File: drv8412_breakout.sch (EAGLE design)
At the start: 1 part

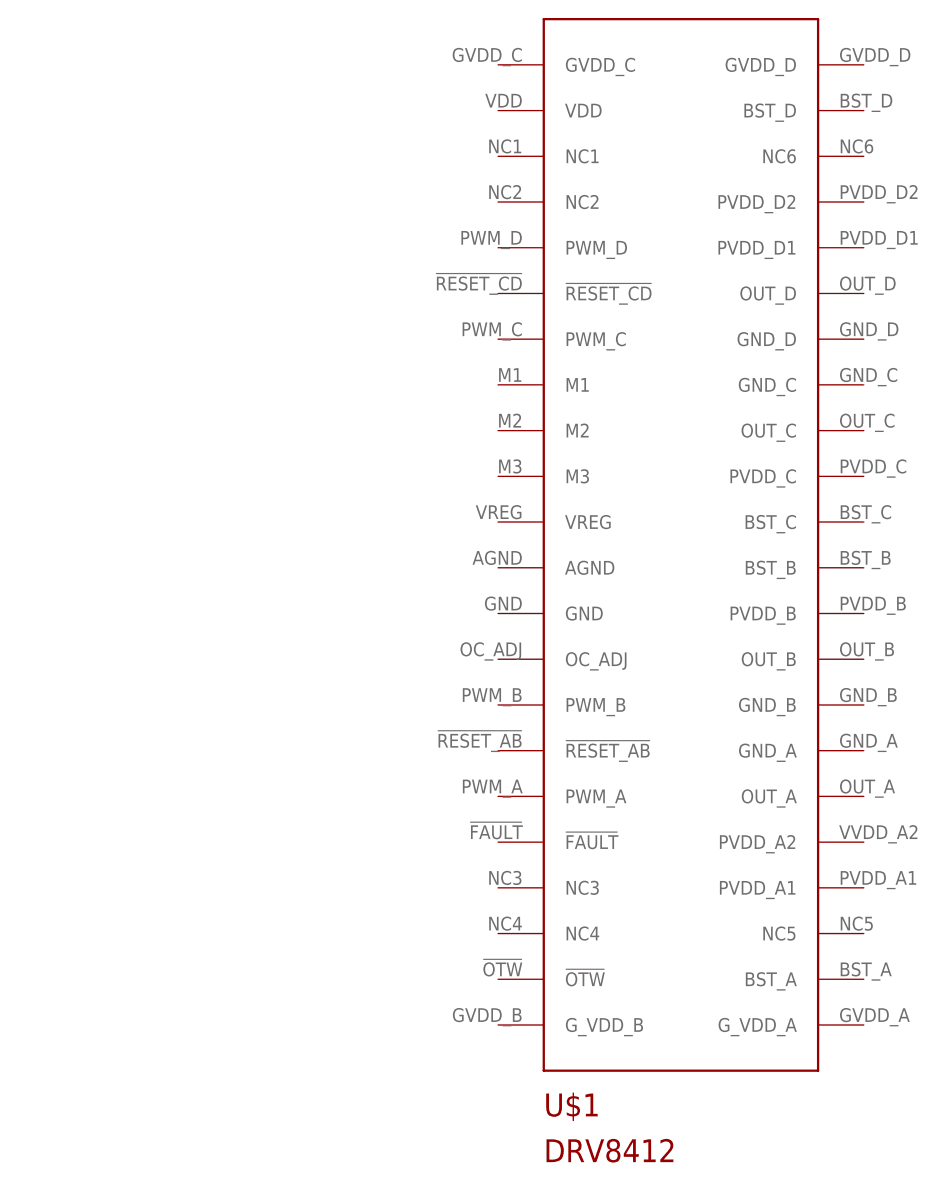
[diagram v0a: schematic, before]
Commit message: Added schematic and board layout
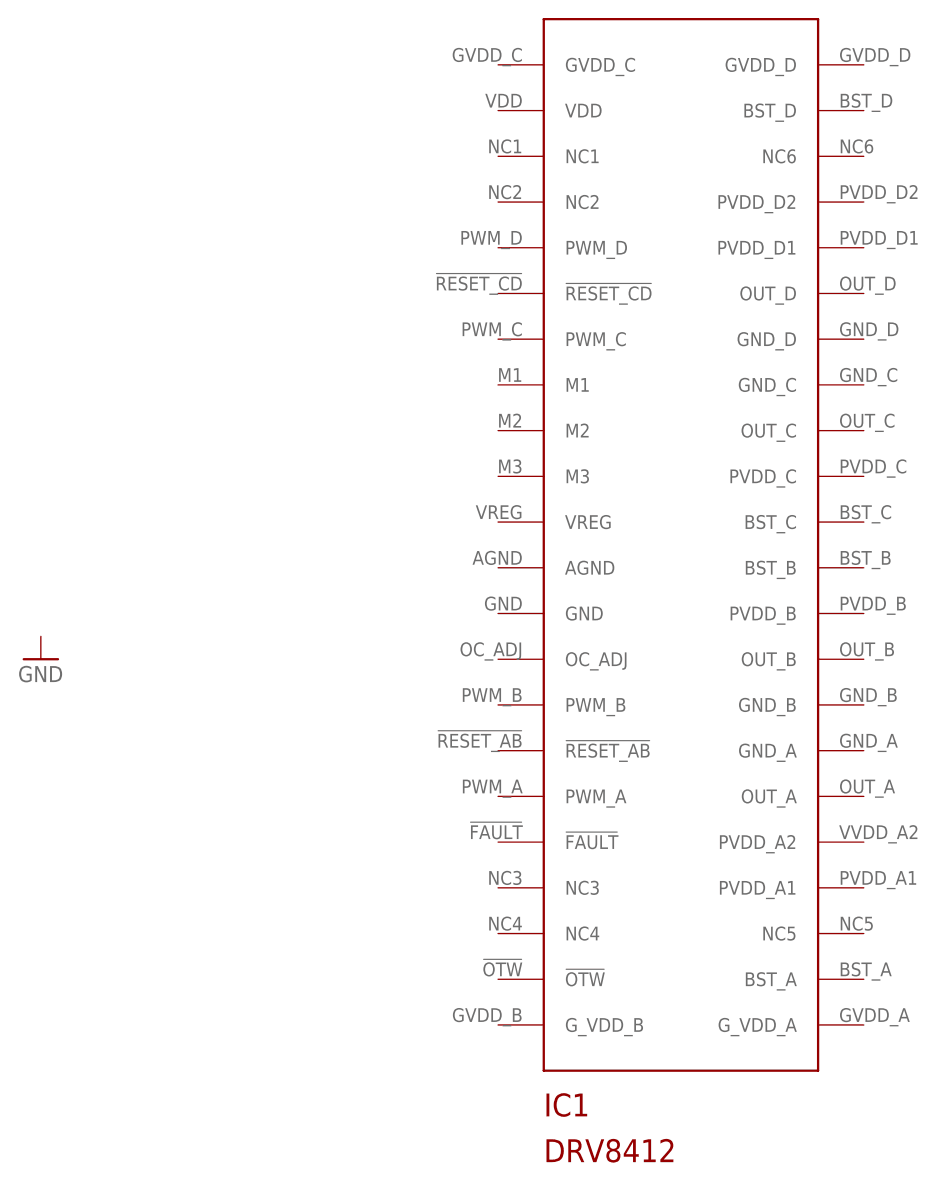
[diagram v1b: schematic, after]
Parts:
- renumbered U$1 to IC1
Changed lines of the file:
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@@
 <layer number="48" name="Document" color="7" fill="1" visible="no" active="no"/>
 <layer number="49" name="Reference" color="7" fill="1" visible="no" active="no"/>
+<layer number="50" name="dxf" color="7" fill="1" visible="no" active="no"/>
 <layer number="51" name="tDocu" color="7" fill="1" visible="no" active="no"/>
 <layer number="52" name="bDocu" color="7" fill="1" visible="no" active="no"/>
+<layer number="53" name="tGND_GNDA" color="7" fill="9" visible="no" active="no"/>
+<layer number="54" name="bGND_GNDA" color="1" fill="9" visible="no" active="no"/>
+<layer number="56" name="wert" color="7" fill="1" visible="no" active="no"/>
 <layer number="90" name="Modules" color="5" fill="1" visible="yes" active="yes"/>
 <layer number="91" name="Nets" color="2" fill="1" visible="yes" active="yes"/>
@@
 <layer number="97" name="Info" color="7" fill="1" visible="yes" active="yes"/>
 <layer number="98" name="Guide" color="6" fill="1" visible="yes" active="yes"/>
+<layer number="100" name="Muster" color="7" fill="1" visible="no" active="no"/>
+<layer number="101" name="Patch_Top" color="12" fill="4" visible="yes" active="yes"/>
+<layer number="102" name="Vscore" color="7" fill="1" visible="yes" active="yes"/>
+<layer number="103" name="tMap" color="7" fill="1" visible="yes" active="yes"/>
+<layer number="104" name="Name" color="16" fill="1" visible="yes" active="yes"/>
+<layer number="105" name="tPlate" color="7" fill="1" visible="yes" active="yes"/>
+<layer number="106" name="bPlate" color="7" fill="1" visible="yes" active="yes"/>
+<layer number="107" name="Crop" color="7" fill="1" visible="yes" active="yes"/>
+<layer number="108" name="tplace-old" color="10" fill="1" visible="no" active="yes"/>
+<layer number="109" name="ref-old" color="11" fill="1" visible="no" active="yes"/>
+<layer number="116" name="Patch_BOT" color="9" fill="4" visible="yes" active="yes"/>
+<layer number="121" name="_tsilk" color="7" fill="1" visible="yes" active="yes"/>
+<layer number="122" name="_bsilk" color="7" fill="1" visible="yes" active="yes"/>
+<layer number="125" name="_tNames" color="7" fill="1" visible="yes" active="yes"/>
+<layer number="144" name="Drill_legend" color="7" fill="1" visible="yes" active="yes"/>
+<layer number="151" name="HeatSink" color="7" fill="1" visible="yes" active="yes"/>
+<layer number="199" name="Contour" color="7" fill="1" visible="yes" active="yes"/>
+<layer number="200" name="200bmp" color="1" fill="10" visible="yes" active="yes"/>
+<layer number="201" name="201bmp" color="2" fill="10" visible="yes" active="yes"/>
+<layer number="202" name="202bmp" color="3" fill="10" visible="yes" active="yes"/>
+<layer number="203" name="203bmp" color="4" fill="10" visible="yes" active="yes"/>
+<layer number="204" name="204bmp" color="5" fill="10" visible="yes" active="yes"/>
+<layer number="205" name="205bmp" color="6" fill="10" visible="yes" active="yes"/>
+<layer number="206" name="206bmp" color="7" fill="10" visible="yes" active="yes"/>
+<layer number="207" name="207bmp" color="8" fill="10" visible="yes" active="yes"/>
+<layer number="208" name="208bmp" color="9" fill="10" visible="yes" active="yes"/>
+<layer number="209" name="209bmp" color="7" fill="1" visible="yes" active="yes"/>
+<layer number="210" name="210bmp" color="7" fill="1" visible="yes" active="yes"/>
+<layer number="211" name="211bmp" color="7" fill="1" visible="yes" active="yes"/>
+<layer number="212" name="212bmp" color="7" fill="1" visible="yes" active="yes"/>
+<layer number="213" name="213bmp" color="7" fill="1" visible="yes" active="yes"/>
+<layer number="214" name="214bmp" color="7" fill="1" visible="yes" active="yes"/>
+<layer number="215" name="215bmp" color="7" fill="1" visible="yes" active="yes"/>
+<layer number="216" name="216bmp" color="7" fill="1" visible="yes" active="yes"/>
+<layer number="217" name="217bmp" color="18" fill="1" visible="no" active="no"/>
+<layer number="218" name="218bmp" color="19" fill="1" visible="no" active="no"/>
+<layer number="219" name="219bmp" color="20" fill="1" visible="no" active="no"/>
+<layer number="220" name="220bmp" color="21" fill="1" visible="no" active="no"/>
+<layer number="221" name="221bmp" color="22" fill="1" visible="no" active="no"/>
+<layer number="222" name="222bmp" color="23" fill="1" visible="no" active="no"/>
+<layer number="223" name="223bmp" color="24" fill="1" visible="no" active="no"/>
+<layer number="224" name="224bmp" color="25" fill="1" visible="no" active="no"/>
+<layer number="250" name="Descript" color="3" fill="1" visible="no" active="no"/>
+<layer number="251" name="SMDround" color="12" fill="11" visible="no" active="no"/>
+<layer number="254" name="cooling" color="7" fill="1" visible="yes" active="yes"/>
 </layers>
 <schematic xreflabel="%F%N/%S.%C%R" xrefpart="/%S.%C%R">
@@
 </classes>
 <parts>
-<part name="U$1" library="DRV8412" deviceset="DRV8412" device="TSSOP44"/>
+<part name="IC1" library="DRV8412" deviceset="DRV8412" device="TSSOP44"/>
+<part name="GND1" library="SparkFun-Aesthetics" deviceset="GND" device=""/>
 </parts>
 <sheets>
@@
 </plain>
 <instances>
-<instance part="U$1" gate="G$1" x="0" y="0"/>
+<instance part="IC1" gate="G$1" x="0" y="0"/>
+<instance part="GND1" gate="1" x="-71.12" y="-15.24"/>
 </instances>
 <busses>
